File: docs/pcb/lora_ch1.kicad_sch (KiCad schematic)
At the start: 42 parts

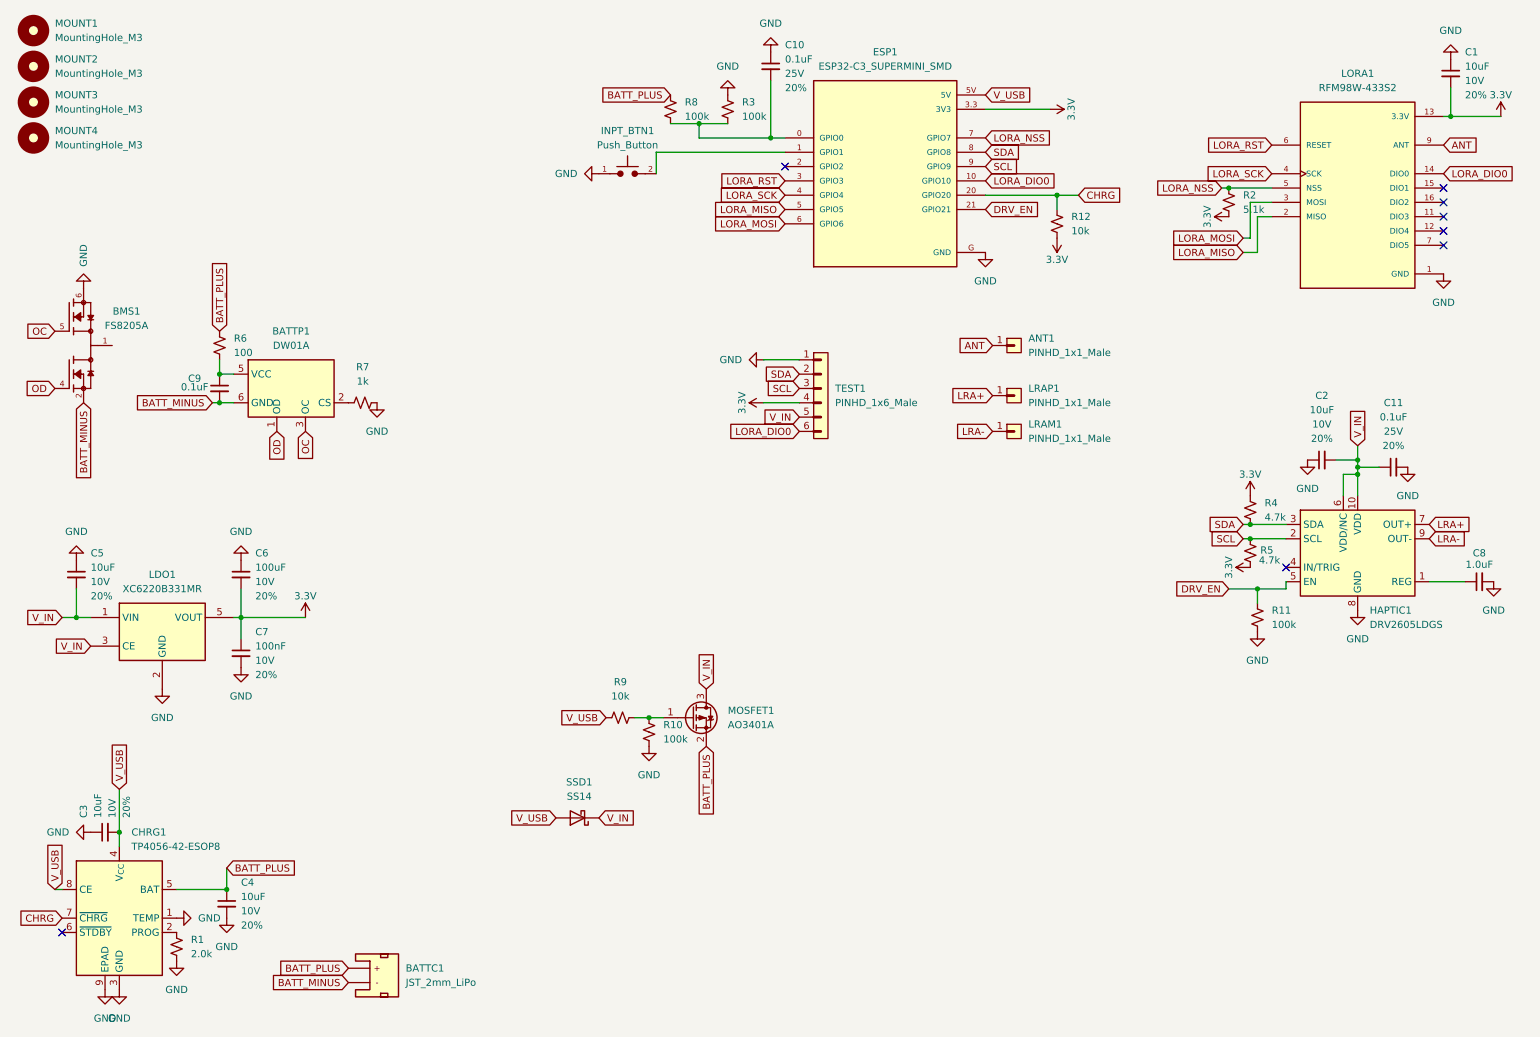
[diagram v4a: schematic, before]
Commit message: PCB rework, added DIO1 connection to GPIO3, changed DIO0 location to GPIO2. Changed the charging controller from TP4056 to BQ24075RGT.
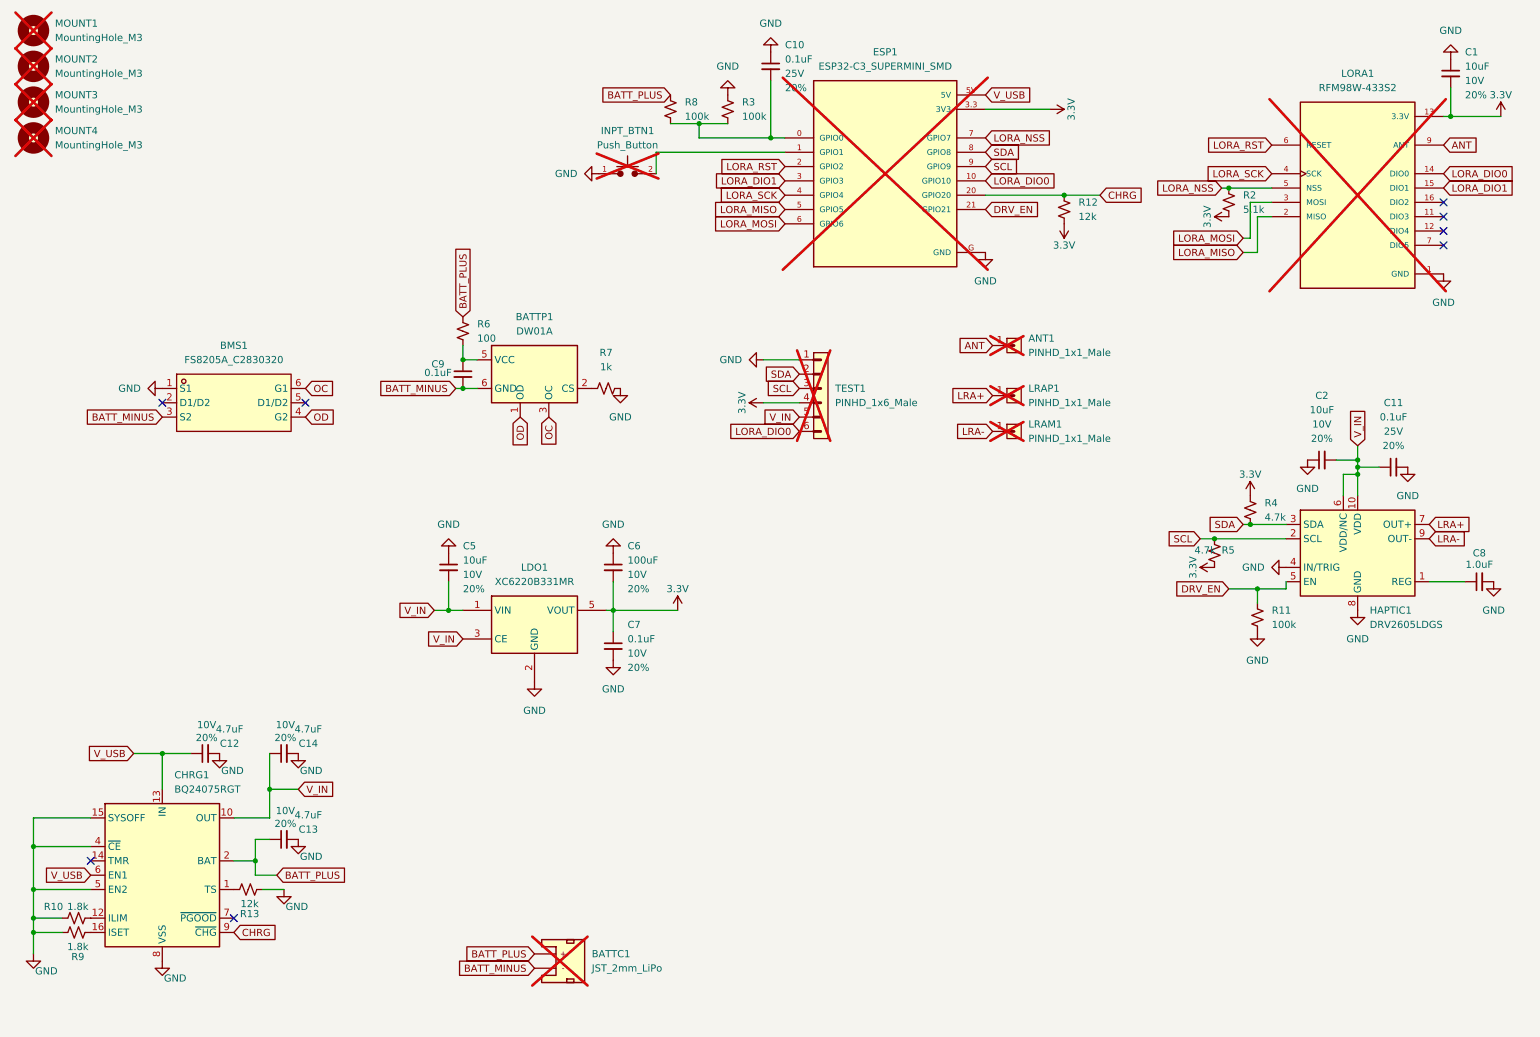
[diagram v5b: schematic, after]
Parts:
- removed BMS1: FS8205A, FS8205A:SOP65P640X120-8N, symbol FS8205A:FS8205A
- removed C3, C4: 10uF, PCM_SparkFun-Capacitor:C_0603_1608Metric, symbol PCM_SparkFun-Capacitor:10uF_0603_10V_20%
- removed CHRG1: TP4056-42-ESOP8, Package_SO:SOIC-8-1EP_3.9x4.9mm_P1.27mm_EP2.41x3.3mm_ThermalVias, symbol Battery_Management:TP4056-42-ESOP8
- removed MOSFET1: AO3401A, Package_TO_SOT_SMD:SOT-23, symbol Transistor_FET:AO3401A
- removed R1: 2.0k, PCM_SparkFun-Resistor:R_0603_1608Metric, symbol PCM_SparkFun-Resistor:2.0k_0603
- removed R10: 100k, PCM_SparkFun-Resistor:R_0603_1608Metric, symbol PCM_SparkFun-Resistor:100k_0603
- removed R12, R9: 10k, PCM_SparkFun-Resistor:R_0603_1608Metric, symbol PCM_SparkFun-Resistor:10k_0603
- removed SSD1: SS14, Diode_SMD:D_SMA, symbol Diode:SS14
- added BMS1: FS8205A_C2830320, easyeda2kicad:SOT-23-6_L2.9-W1.6-P0.95-LS2.8-BR, symbol FS8205A:FS8205A_C2830320
- added C12, C13, C14: 4.7uF, PCM_SparkFun-Capacitor:C_0603_1608Metric, symbol PCM_SparkFun-Capacitor:10uF_0603_10V_20%
- added CHRG1: BQ24075RGT, Package_DFN_QFN:VQFN-16-1EP_3x3mm_P0.5mm_EP1.6x1.6mm, symbol Battery_Management:BQ24075RGT
- added R10, R9: 1.8k, PCM_SparkFun-Resistor:R_0603_1608Metric, symbol PCM_SparkFun-Resistor:1k_0603
- added R12: 12k, PCM_SparkFun-Resistor:R_0603_1608Metric, symbol PCM_SparkFun-Resistor:100k_0603
- added R13: 12k, PCM_SparkFun-Resistor:R_0603_1608Metric, symbol PCM_SparkFun-Resistor:1k_0603
- ANT1, BATTC1, ESP1, INPT_BTN1, LORA1, LRAM1, LRAP1, MOUNT1, MOUNT2, MOUNT3, MOUNT4, TEST1: now not fitted
- C7: value 100nF -> 0.1uF
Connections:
- net 3.3V: now also R12.1
- net BATT_MINUS: now also BMS1.3 (S2)
- net BATT_PLUS: now also C13.1, CHRG1.2 (BAT), CHRG1.3 (BAT)
- net CHRG: now also CHRG1.9 (~{CHG}), R12.2
- net GND: now also HAPTIC1.4 (IN/TRIG), BMS1.1 (S1), C12.2, C13.2, C14.2, CHRG1.15 (SYSOFF), CHRG1.17 (VSS), CHRG1.4 (~{CE}), CHRG1.5 (EN2), CHRG1.8 (VSS), R10.1, R13.1, R9.2
- net LORA_RST: now also ESP1.2 (GPIO2); no longer ESP1.3 (GPIO3)
- net OC: now also BMS1.6 (G1)
- net OD: now also BMS1.4 (G2)
- net V_IN: now also C14.1, CHRG1.10 (OUT), CHRG1.11 (OUT)
- net V_USB: now also C12.1, CHRG1.13 (IN), CHRG1.6 (EN1)
- net LORA_DIO1: now reaches LORA1.15 (DIO1), LORA1.15_1 (DIO1)
- net LORA_DIO1: now also ESP1.3 (GPIO3)
- new net: CHRG1.12 (ILIM), R10.2
- new net: CHRG1.1 (TS), R13.2
- new net: CHRG1.16 (ISET), R9.1
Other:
- moved on the sheet: BATTP1, C5, C6, C7, C9, LDO1, R5, R6, R7
